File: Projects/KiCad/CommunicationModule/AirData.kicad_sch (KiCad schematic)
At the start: 23 parts, among them J1 Conn_01x04_Pin, J2 Conn_01x04_Pin, J3 Micro_SD_Card_Det_Hirose_DM3AT, U1 ABX00012, U2 MCP2562-E-P, U3 LT1584-3.3, U4 TLP222A, U5 MCP2515-I/P, Y1 8MHz

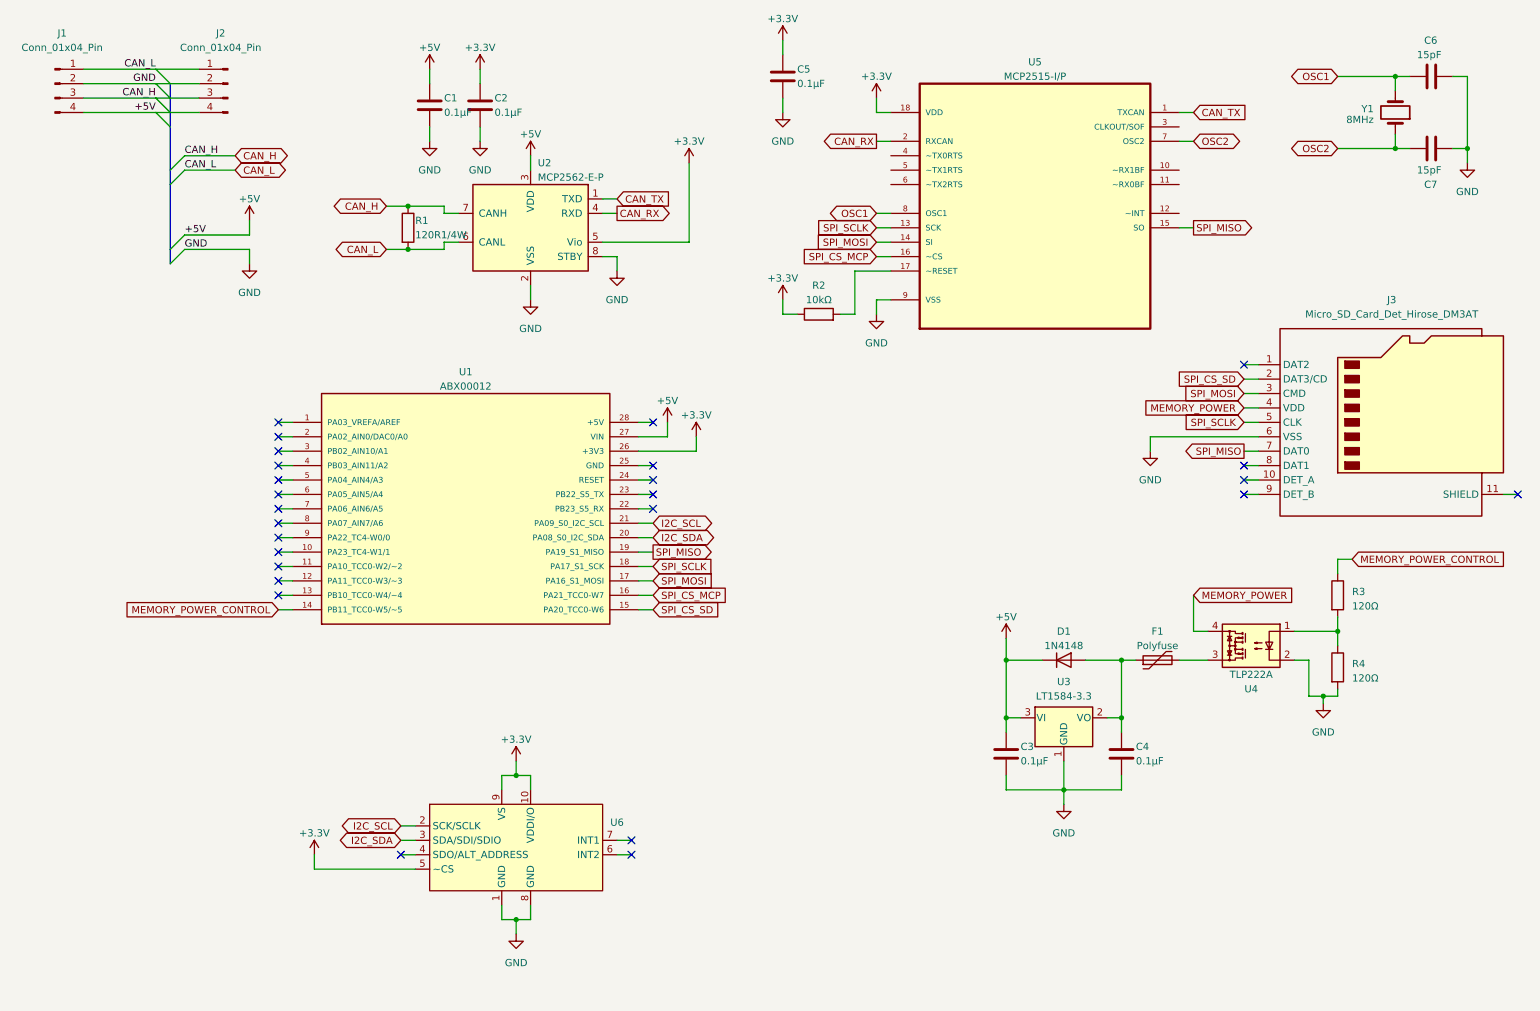
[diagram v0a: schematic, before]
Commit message: ミッションモジュール, エアデータ通信モジュール, システムデータ通信モジュールのKiCadを追加
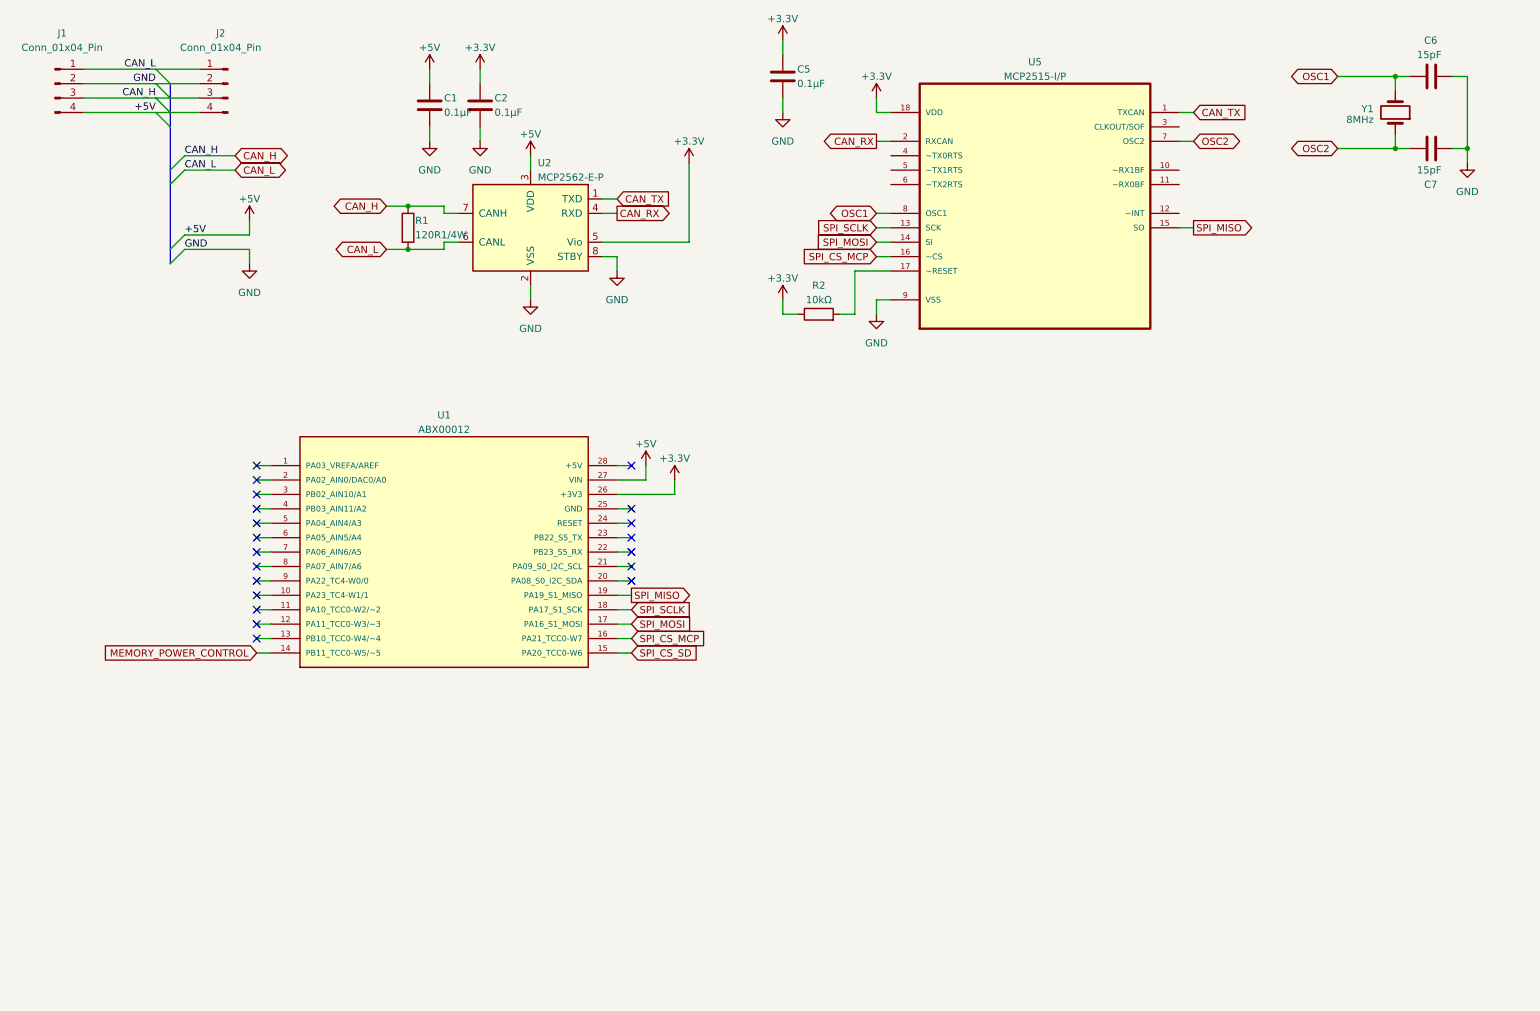
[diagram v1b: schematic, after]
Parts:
- removed C3, C4: 0.1μF, Capacitor_SMD:C_0805_2012Metric_Pad1.18x1.45mm_HandSolder, symbol Device:C
- removed D1: 1N4148, Diode_THT:D_DO-35_SOD27_P7.62mm_Horizontal, symbol Diode:1N4148
- removed F1: Polyfuse, Fuse:Fuse_BelFuse_0ZRE0005FF_L8.3mm_W3.8mm, symbol Device:Polyfuse
- removed J3: Micro_SD_Card_Det_Hirose_DM3AT, Connector_Card:microSD_HC_Hirose_DM3AT-SF-PEJM5, symbol Connector:Micro_SD_Card_Det_Hirose_DM3AT
- removed R3, R4: 120Ω, Resistor_SMD:R_0805_2012Metric_Pad1.20x1.40mm_HandSolder, symbol Device:R
- removed U3: LT1584-3.3, Package_TO_SOT_THT:TO-220-3_Vertical, symbol Regulator_Linear:LT1584-3.3
- removed U4: TLP222A, Package_DIP:DIP-4_W7.62mm, symbol Relay_SolidState:TLP222A
- removed U6: ~, StrawberryLinux_ADXL375_Module:ADXL375, symbol StrawberryLinux_ADXL375_Module:ADXL375
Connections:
- net I2C_SCL: no longer names the net of U1.21 (PA09_S0_I2C_SCL)
- net I2C_SDA: no longer names the net of U1.20 (PA08_S0_I2C_SDA)
- no-connect marks 26 -> 20
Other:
- moved on the sheet: U1

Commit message: 全モジュールのkicadを一通り作った
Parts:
- added D1, D2, D3, D4, D5: LED, LED_SMD:LED_1206_3216Metric_Pad1.42x1.75mm_HandSolder, symbol Device:LED
- added R3: 2kΩ, Resistor_SMD:R_0805_2012Metric_Pad1.20x1.40mm_HandSolder, symbol Device:R
- added R4, R5, R6, R7: 100Ω, Resistor_SMD:R_0805_2012Metric_Pad1.20x1.40mm_HandSolder, symbol Device:R
- added SW1: SW_Push, Button_Switch_THT:SW_PUSH_6mm, symbol Switch:SW_Push
- R2: footprint (none) -> Resistor_SMD:R_0805_2012Metric_Pad1.20x1.40mm_HandSolder
- renumbered C5 to C3, C6 to C4, C7 to C5, U5 to U3
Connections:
- net +5V: now also R3.1
- net GND: now also D1.1 (K), D2.1 (K), D3.1 (K), D4.1 (K), D5.1 (K), SW1.1
- net CAN_RECEIVE_STATUS: now reaches U1.10 (PA23_TC4-W1/1)
- net CAN_RECEIVE_STATUS: now also R4.1
- net CAN_SEND_STATUS: now reaches U1.11 (PA10_TCC0-W2/~2)
- net CAN_SEND_STATUS: now also R5.1
- net LORA_RECEIVE_STATUS: now reaches U1.12 (PA11_TCC0-W3/~3)
- net LORA_RECEIVE_STATUS: now also R6.1
- net LORA_SEND_STATUS: now reaches U1.13 (PB10_TCC0-W4/~4)
- net LORA_SEND_STATUS: now also R7.1
- net DEBUG_MODE: now reaches U1.9 (PA22_TC4-W0/0)
- net DEBUG_MODE: now also SW1.2
- net MEMORY_POWER_CONTROL: no longer names the net of U1.14 (PB11_TCC0-W5/~5)
- net SPI_CS_SD: no longer names the net of U1.15 (PA20_TCC0-W6)
- new net: D1.2 (A), R3.2
- new net: D5.2 (A), R7.2
- new net: D2.2 (A), R4.2
- new net: D4.2 (A), R6.2
- new net: D3.2 (A), R5.2
- no-connect marks 20 -> 17

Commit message: 一通り部品を選定
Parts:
- C4, C5: footprint Capacitor_SMD:C_0805_2012Metric_Pad1.18x1.45mm_HandSolder -> Capacitor_SMD:C_0603_1608Metric_Pad1.08x0.95mm_HandSolder
- D1: value LED -> RED; footprint LED_SMD:LED_1206_3216Metric_Pad1.42x1.75mm_HandSolder -> LED_SMD:LED_0603_1608Metric_Pad1.05x0.95mm_HandSolder
- D2, D3, D4, D5: value LED -> ORANGE; footprint LED_SMD:LED_1206_3216Metric_Pad1.42x1.75mm_HandSolder -> LED_SMD:LED_0603_1608Metric_Pad1.05x0.95mm_HandSolder
- R1: value 120R1/4W -> 120Ω; footprint Resistor_SMD:R_0805_2012Metric_Pad1.20x1.40mm_HandSolder -> Resistor_SMD:R_0603_1608Metric_Pad0.98x0.95mm_HandSolder
- R2, R4, R5, R6, R7: footprint Resistor_SMD:R_0805_2012Metric_Pad1.20x1.40mm_HandSolder -> Resistor_SMD:R_0603_1608Metric_Pad0.98x0.95mm_HandSolder
- R3: value 2kΩ -> 620Ω; footprint Resistor_SMD:R_0805_2012Metric_Pad1.20x1.40mm_HandSolder -> Resistor_SMD:R_0603_1608Metric_Pad0.98x0.95mm_HandSolder
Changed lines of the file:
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@@
       (effects (font (size 1.27 1.27)) (justify right))
     )
-    (property "Value" "LED" (at 214.63 120.9674 90)
-      (effects (font (size 1.27 1.27)) (justify right))
-    )
-    (property "Footprint" "LED_SMD:LED_1206_3216Metric_Pad1.42x1.75mm_HandSolder" (at 210.82 118.11 0)
+    (property "Value" "RED" (at 214.63 120.9674 90)
+      (effects (font (size 1.27 1.27)) (justify right))
+    )
+    (property "Footprint" "LED_SMD:LED_0603_1608Metric_Pad1.05x0.95mm_HandSolder" (at 210.82 118.11 0)
       (effects (font (size 1.27 1.27)) hide)
     )
@@
       (effects (font (size 1.27 1.27)) (justify right))
     )
-    (property "Value" "LED" (at 254 120.9674 90)
-      (effects (font (size 1.27 1.27)) (justify right))
-    )
-    (property "Footprint" "LED_SMD:LED_1206_3216Metric_Pad1.42x1.75mm_HandSolder" (at 250.19 118.11 0)
+    (property "Value" "ORANGE" (at 254 120.9674 90)
+      (effects (font (size 1.27 1.27)) (justify right))
+    )
+    (property "Footprint" "LED_SMD:LED_0603_1608Metric_Pad1.05x0.95mm_HandSolder" (at 250.19 118.11 0)
       (effects (font (size 1.27 1.27)) hide)
     )
@@
       (effects (font (size 1.27 1.27)) (justify right))
     )
-    (property "Value" "LED" (at 223.52 120.9674 90)
-      (effects (font (size 1.27 1.27)) (justify right))
-    )
-    (property "Footprint" "LED_SMD:LED_1206_3216Metric_Pad1.42x1.75mm_HandSolder" (at 219.71 118.11 0)
+    (property "Value" "ORANGE" (at 223.52 120.9674 90)
+      (effects (font (size 1.27 1.27)) (justify right))
+    )
+    (property "Footprint" "LED_SMD:LED_0603_1608Metric_Pad1.05x0.95mm_HandSolder" (at 219.71 118.11 0)
       (effects (font (size 1.27 1.27)) hide)
     )
@@
       (effects (font (size 1.27 1.27)))
     )
-    (property "Footprint" "Resistor_SMD:R_0805_2012Metric_Pad1.20x1.40mm_HandSolder" (at 156.21 70.358 90)
+    (property "Footprint" "Resistor_SMD:R_0603_1608Metric_Pad0.98x0.95mm_HandSolder" (at 156.21 70.358 90)
       (effects (font (size 1.27 1.27)) hide)
     )
@@
       (effects (font (size 1.27 1.27)) (justify left))
     )
-    (property "Footprint" "Capacitor_SMD:C_0805_2012Metric_Pad1.18x1.45mm_HandSolder" (at 260.35 38.4048 0)
+    (property "Footprint" "Capacitor_SMD:C_0603_1608Metric_Pad1.08x0.95mm_HandSolder" (at 260.35 38.4048 0)
       (effects (font (size 1.27 1.27)) hide)
     )
@@
       (effects (font (size 1.27 1.27)) (justify right))
     )
-    (property "Value" "LED" (at 243.84 120.9674 90)
-      (effects (font (size 1.27 1.27)) (justify right))
-    )
-    (property "Footprint" "LED_SMD:LED_1206_3216Metric_Pad1.42x1.75mm_HandSolder" (at 240.03 118.11 0)
+    (property "Value" "ORANGE" (at 243.84 120.9674 90)
+      (effects (font (size 1.27 1.27)) (justify right))
+    )
+    (property "Footprint" "LED_SMD:LED_0603_1608Metric_Pad1.05x0.95mm_HandSolder" (at 240.03 118.11 0)
       (effects (font (size 1.27 1.27)) hide)
     )
@@
       (effects (font (size 1.27 1.27)) (justify left))
     )
-    (property "Footprint" "Resistor_SMD:R_0805_2012Metric_Pad1.20x1.40mm_HandSolder" (at 217.932 107.95 90)
+    (property "Footprint" "Resistor_SMD:R_0603_1608Metric_Pad0.98x0.95mm_HandSolder" (at 217.932 107.95 90)
       (effects (font (size 1.27 1.27)) hide)
     )
@@
       (effects (font (size 1.27 1.27)) (justify left))
     )
-    (property "Footprint" "Resistor_SMD:R_0805_2012Metric_Pad1.20x1.40mm_HandSolder" (at 238.252 107.95 90)
+    (property "Footprint" "Resistor_SMD:R_0603_1608Metric_Pad0.98x0.95mm_HandSolder" (at 238.252 107.95 90)
       (effects (font (size 1.27 1.27)) hide)
     )
@@
       (effects (font (size 1.27 1.27)) (justify left))
     )
-    (property "Value" "2kΩ" (at 213.36 109.2199 0)
-      (effects (font (size 1.27 1.27)) (justify left))
-    )
-    (property "Footprint" "Resistor_SMD:R_0805_2012Metric_Pad1.20x1.40mm_HandSolder" (at 209.042 107.95 90)
+    (property "Value" "620Ω" (at 213.36 109.2199 0)
+      (effects (font (size 1.27 1.27)) (justify left))
+    )
+    (property "Footprint" "Resistor_SMD:R_0603_1608Metric_Pad0.98x0.95mm_HandSolder" (at 209.042 107.95 90)
       (effects (font (size 1.27 1.27)) hide)
     )
@@
       (effects (font (size 1.27 1.27)) (justify left))
     )
-    (property "Footprint" "Resistor_SMD:R_0805_2012Metric_Pad1.20x1.40mm_HandSolder" (at 228.092 107.95 90)
+    (property "Footprint" "Resistor_SMD:R_0603_1608Metric_Pad0.98x0.95mm_HandSolder" (at 228.092 107.95 90)
       (effects (font (size 1.27 1.27)) hide)
     )
@@
       (effects (font (size 1.27 1.27)) (justify left))
     )
-    (property "Footprint" "Capacitor_SMD:C_0805_2012Metric_Pad1.18x1.45mm_HandSolder" (at 260.35 25.7048 0)
+    (property "Footprint" "Capacitor_SMD:C_0603_1608Metric_Pad1.08x0.95mm_HandSolder" (at 260.35 25.7048 0)
       (effects (font (size 1.27 1.27)) hide)
     )
@@
       (effects (font (size 1.27 1.27)) (justify right))
     )
-    (property "Value" "LED" (at 233.68 120.9674 90)
-      (effects (font (size 1.27 1.27)) (justify right))
-    )
-    (property "Footprint" "LED_SMD:LED_1206_3216Metric_Pad1.42x1.75mm_HandSolder" (at 229.87 118.11 0)
+    (property "Value" "ORANGE" (at 233.68 120.9674 90)
+      (effects (font (size 1.27 1.27)) (justify right))
+    )
+    (property "Footprint" "LED_SMD:LED_0603_1608Metric_Pad1.05x0.95mm_HandSolder" (at 229.87 118.11 0)
       (effects (font (size 1.27 1.27)) hide)
     )
@@
       (effects (font (size 1.27 1.27)) (justify left))
     )
-    (property "Value" "120R1/4W" (at 85.09 54.61 0)
-      (effects (font (size 1.27 1.27)) (justify left))
-    )
-    (property "Footprint" "Resistor_SMD:R_0805_2012Metric_Pad1.20x1.40mm_HandSolder" (at 82.042 53.34 90)
+    (property "Value" "120Ω" (at 85.09 54.61 0)
+      (effects (font (size 1.27 1.27)) (justify left))
+    )
+    (property "Footprint" "Resistor_SMD:R_0603_1608Metric_Pad0.98x0.95mm_HandSolder" (at 82.042 53.34 90)
       (effects (font (size 1.27 1.27)) hide)
     )
@@
       (effects (font (size 1.27 1.27)) (justify left))
     )
-    (property "Footprint" "Resistor_SMD:R_0805_2012Metric_Pad1.20x1.40mm_HandSolder" (at 248.412 107.95 90)
-      (effects (font (size 1.27 1.27)) hide)
-    )
+    (property "Footprint" "Resistor_SMD:R_0603_1608Metric_Pad0.98x0.95mm_HandSolder" (at 248.412 107.95 90)
+      (effects (font (size 1.27 1.27)) hide)
+    )
